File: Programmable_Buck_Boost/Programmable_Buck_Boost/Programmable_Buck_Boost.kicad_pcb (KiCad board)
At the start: 2 copper layers, 29 parts, among them J2 DC INPUT, Q5 IRF3205, Q6 IRF3205, Q7 2N7002, U4 TL494, U6 IR2101

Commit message: Finalize Schematic
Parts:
- added C1: C0603/1nF, Capacitor_SMD:C_0603_1608Metric, F.Cu at (160.4, 80.4)
- added C10: C0805/22uF, Capacitor_SMD:C_0603_1608Metric, F.Cu at (191.1, 112.2)
- added C11: C0603/0.1uF, Capacitor_SMD:C_0603_1608Metric, F.Cu at (191.1, 114.7)
- added C13: C0805/22uF, Capacitor_SMD:C_0603_1608Metric, F.Cu at (191.1, 117.2)
- added C14: C0805/22uF, Capacitor_SMD:C_0603_1608Metric, F.Cu at (191.1, 119.7)
- added C15: C0603/10uF, Capacitor_SMD:C_0603_1608Metric, F.Cu at (160.4, 93.0)
- added C16: C0603/470nF, Capacitor_SMD:C_0603_1608Metric, F.Cu at (164.4, 80.4)
- added C17: C0603/100nF, Capacitor_SMD:C_0603_1608Metric, F.Cu at (164.4, 82.9)
- added C18: C0603/68pF, Capacitor_SMD:C_0603_1608Metric, F.Cu at (164.4, 85.4)
- added C19: C0603/1uF, Capacitor_SMD:C_0603_1608Metric, F.Cu at (164.4, 87.9)
- added C2: C0603/100nF, Capacitor_SMD:C_0603_1608Metric, F.Cu at (144.6, 127.5)
- added C2: C0603/10uF, Capacitor_SMD:C_0603_1608Metric, F.Cu at (160.4, 82.9)
- added C21: C0603/100nF, Capacitor_SMD:C_0603_1608Metric, F.Cu at (164.4, 90.5)
- added C22: C0603/1uF, Capacitor_SMD:C_0603_1608Metric, F.Cu at (191.1, 122.2)
- added C3: C0603/1uF, Capacitor_SMD:C_0603_1608Metric, F.Cu at (160.4, 85.4)
- added C4: C0603/0.1uF, Capacitor_SMD:C_0603_1608Metric, F.Cu at (160.4, 87.9)
- added C5: C0603/0.1uF, Capacitor_SMD:C_0603_1608Metric, F.Cu at (160.4, 90.5)
- added C5: C0603/100nF, Capacitor_SMD:C_0603_1608Metric, F.Cu at (144.6, 130.1)
- added C6: C0603/10uF, Capacitor_SMD:C_0603_1608Metric, F.Cu at (144.6, 132.6)
- added C7: C0603/1uF, Capacitor_SMD:C_0603_1608Metric, F.Cu at (144.6, 135.1)
- added C8: C0603/10uF, Capacitor_SMD:C_0603_1608Metric, F.Cu at (144.6, 137.6)
- added C9: C0805/22uF, Capacitor_SMD:C_0603_1608Metric, F.Cu at (191.1, 109.7)
- added D2: SS34, Diode_SMD:D_SMA, F.Cu at (174.6, 126.0)
- added R1: R0603/4.7K, Resistor_SMD:R_0603_1608Metric, F.Cu at (144.6, 140.1)
- added R10: R0603/100K, Resistor_SMD:R_0603_1608Metric, F.Cu at (195.1, 117.2)
- added R11: R0603/100K, Resistor_SMD:R_0603_1608Metric, F.Cu at (195.1, 119.7)
- added R2: R0603/100K, Resistor_SMD:R_0603_1608Metric, F.Cu at (148.6, 127.5)
- added R3: R0603/51K, Resistor_SMD:R_0603_1608Metric, F.Cu at (148.6, 130.1)
- added R4: R0603/100K, Resistor_SMD:R_0603_1608Metric, F.Cu at (148.6, 132.6)
- added R5: R0603/56k, Resistor_SMD:R_0603_1608Metric, F.Cu at (148.6, 135.1)
- added R6: R0603/4.7K, Resistor_SMD:R_0603_1608Metric, F.Cu at (148.6, 137.6)
- added R7: R0603/100K, Resistor_SMD:R_0603_1608Metric, F.Cu at (195.1, 109.7)
- added R8: R0603/100K, Resistor_SMD:R_0603_1608Metric, F.Cu at (195.1, 112.2)
- added R9: R0603/0.82, Resistor_SMD:R_0603_1608Metric, F.Cu at (195.1, 114.7)
- added SW1: RotaryEncoder_Switch, Rotary_Encoder:RotaryEncoder_Alps_EC11E-Switch_Vertical_H20mm, F.Cu at (119.8, 136.8)
- added U1: MP1470, Package_TO_SOT_SMD:TSOT-23-6, F.Cu at (153.2, 128.7)
- added U2: MSPS003F4SPW20R, Package_SO:TSSOP-20_4.4x6.5mm_P0.65mm, F.Cu at (169.0, 98.5)
- added U3: MCP601-xOT, Package_TO_SOT_SMD:SOT-23-5, F.Cu at (153.2, 133.3)
- added U5: EG1198, Package_SO:HSOP-8-1EP_3.9x4.9mm_P1.27mm_EP2.3x2.3mm, F.Cu at (163.1, 127.6)
- R36, R39, R40: value R0603/10k -> R0603/100k
- R37: value R0603/220R -> R0603/2.2K
- R53: value RS/0.5R -> RS/0.1R
- R55: value R0603/56k -> R0603/150K
- U4: footprint Package_DIP:CERDIP-16_W7.62mm_SideBrazed_LongPads -> Package_SO:SOIC-16_3.9x9.9mm_P1.27mm
- moved R36 48.7 mm to (140.5, 81.7)
- moved R37 48.7 mm to (140.5, 84.2)
- moved R38 48.7 mm to (140.5, 86.7)
- moved R39 48.7 mm to (140.5, 89.2)
- moved R40 48.7 mm to (140.5, 91.8)
- moved R41 48.7 mm to (144.5, 81.7)
- moved R42 48.7 mm to (144.5, 84.2)
- moved R43 48.7 mm to (144.5, 86.7)
- moved R44 48.7 mm to (144.5, 89.2)
- moved R45 48.7 mm to (144.5, 91.8)
- moved R51 48.7 mm to (152.5, 81.7)
- moved R52 48.7 mm to (152.5, 84.2)
- moved R53 48.7 mm to (152.5, 86.7)
- moved R54 48.7 mm to (152.5, 89.2)
- moved R55 48.7 mm to (152.5, 91.8)
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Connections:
- R36 pad 1: Net-(C17-Pad2) -> /I_SET
- R37 pad 2: Net-(C17-Pad2) -> /I_SET
- R39 pad 1: Net-(U4-1IN-) -> /V_SET
- R40 pad 2: Net-(U4-1IN-) -> /V_SET
- R52 pad 1: V_set -> /V_FB
- R53 pad 2: I_set -> Net-(C20-Pad2)
- R55 pad 1: V_set -> /V_FB
- U4 pad 1: V_fb -> /V_FB
- U4 pad 15: Net-(U4-1IN-) -> /I_SET
- U4 pad 16: I_set -> /I_FB
- U4 pad 2: Net-(U4-1IN-) -> /V_SET

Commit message: Change design
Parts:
- added C11: Cp/470uF/63V, Capacitor_THT:CP_Radial_D12.5mm_P5.00mm, F.Cu at (205.0, 119.6)
- added C12: Cp/47uF/63V, Capacitor_THT:CP_Radial_D8.0mm_P3.50mm, F.Cu at (234.7, 147.2)
- added C2: C0603/33nF, Capacitor_SMD:C_0603_1608Metric, F.Cu at (216.5, 113.8)
- added C20: 220uF/65V, Connector_JST:JST_XH_B5B-XH-AM_1x05_P2.50mm_Vertical, F.Cu at (218.0, 133.5)
- added C22: Cp/470uF/63V, Capacitor_THT:CP_Radial_D12.5mm_P5.00mm, F.Cu at (205.0, 133.7)
- added C23: Cp/470uF/63V, Capacitor_THT:CP_Radial_D12.5mm_P5.00mm, F.Cu at (205.0, 147.7)
- added C24: C0603/1nF, Capacitor_SMD:C_0603_1608Metric, F.Cu at (216.5, 116.3)
- added C25: C0603/100nF, Capacitor_SMD:C_0603_1608Metric, F.Cu at (216.5, 118.8)
- added C26: C0603/100nF, Capacitor_SMD:C_0603_1608Metric, F.Cu at (216.5, 121.4)
- added C27: C0603/100nF, Capacitor_SMD:C_0603_1608Metric, F.Cu at (216.5, 123.9)
- added C28: C0603/100nF, Capacitor_SMD:C_0603_1608Metric, F.Cu at (216.5, 126.4)
- added C29: C0603/100nF, Capacitor_SMD:C_0603_1608Metric, F.Cu at (216.5, 128.9)
- added C30: C0603/100nF, Capacitor_SMD:C_0603_1608Metric, F.Cu at (220.5, 113.8)
- added C31: C0603/100nF, Capacitor_SMD:C_0603_1608Metric, F.Cu at (220.5, 116.3)
- added D3: SS34, Diode_SMD:D_SMA, F.Cu at (227.0, 148.0)
- added J1: Conn_01x05_Pin, Connector_JST:JST_XH_B5B-XH-AM_1x05_P2.50mm_Vertical, F.Cu at (218.0, 141.3)
- added J4: Conn_01x04_Pin, Connector_PinSocket_2.54mm:PinSocket_1x04_P2.54mm_Vertical, F.Cu at (233.8, 132.5)
- added L1: L/47uH /620mA, Inductor_SMD:L_Abracon_ASPI-0425, F.Cu at (229.6, 126.7)
- added R12: R0603/150K, Resistor_SMD:R_0603_1608Metric, F.Cu at (220.5, 121.4)
- added R13: R0603/150K, Resistor_SMD:R_0603_1608Metric, F.Cu at (220.5, 123.9)
- added R14: R0603/150K, Resistor_SMD:R_0603_1608Metric, F.Cu at (220.5, 126.4)
- added R15: R0603/150K, Resistor_SMD:R_0603_1608Metric, F.Cu at (220.5, 128.9)
- added R16: R0603/10K, Resistor_SMD:R_0603_1608Metric, F.Cu at (224.5, 113.8)
- added R17: R0603/10K, Resistor_SMD:R_0603_1608Metric, F.Cu at (224.5, 116.3)
- added R18: R0603/100K, Resistor_SMD:R_0603_1608Metric, F.Cu at (224.5, 118.8)
- added R19: R0603/100K, Resistor_SMD:R_0603_1608Metric, F.Cu at (224.5, 121.4)
- added R9: R0603/100K, Resistor_SMD:R_0603_1608Metric, F.Cu at (220.5, 118.8)
- added REF**: Untitled, Untitled, F.Cu at (125.8, 93.0)
- added U2: XL7005A, Package_SO:SOIC-8-1EP_3.9x4.9mm_P1.27mm_EP2.29x3mm, F.Cu at (218.7, 149.1)
- added U5: STM32F103C8Tx, Package_QFP:LQFP-48_7x7mm_P0.5mm, F.Cu at (232.2, 118.2)
- added U7: MCP601-xOT, Package_TO_SOT_SMD:SOT-23-5, F.Cu at (235.2, 126.3)
- C9: value C0805/22uF -> C0603/10uF
- D2: value SS34 -> SS24
- Q5, Q6: value IRF3205 -> IRFB4110PbF
- R10: value R0603/100K -> R0603/30K
- R11: value R0603/100K -> R0603/3.3K
- R37: value R0603/2.2K -> R0603/100K
- R53: value RS/0.1R -> RS/0.002R
- R7: value R0603/100K -> R0603/75K
- R8: value R0603/100K -> R0603/24K
- moved U6 66.1 mm to (179.7, 85.4), turned to 90 degrees
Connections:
- C10 pad 1: Net-(U1-IN) -> +12V
- C13 pad 1: Net-(C13-Pad1) -> +12V
- C14 pad 1: Net-(C13-Pad1) -> +12V
- C9 pad 1: Net-(C9-Pad1) -> +3.3V
- R10 pad 1: /12VFB -> +12V
- R10 pad 2: Net-(C13-Pad1) -> /12VFB
- R2 pad 2: Net-(U1-IN) -> +12V
- R44 pad 2: +5V -> +12V
- R6 pad 1: /VSETPOINT -> /V_PWM
- R7 pad 1: /3V3FB -> +3.3V
- R7 pad 2: Net-(C9-Pad1) -> /3V3FB
- SW1 pad A: Net-(U2-PA25/A2) -> /ENC_A
- SW1 pad B: Net-(U2-PA24/A3) -> /ENC_B
- U1 pad 3: Net-(U1-IN) -> +12V
- U4 pad 10: Net-(U4-E1) -> Net-(Q7-G)
- U4 pad 9: Net-(U4-E1) -> Net-(Q7-G)

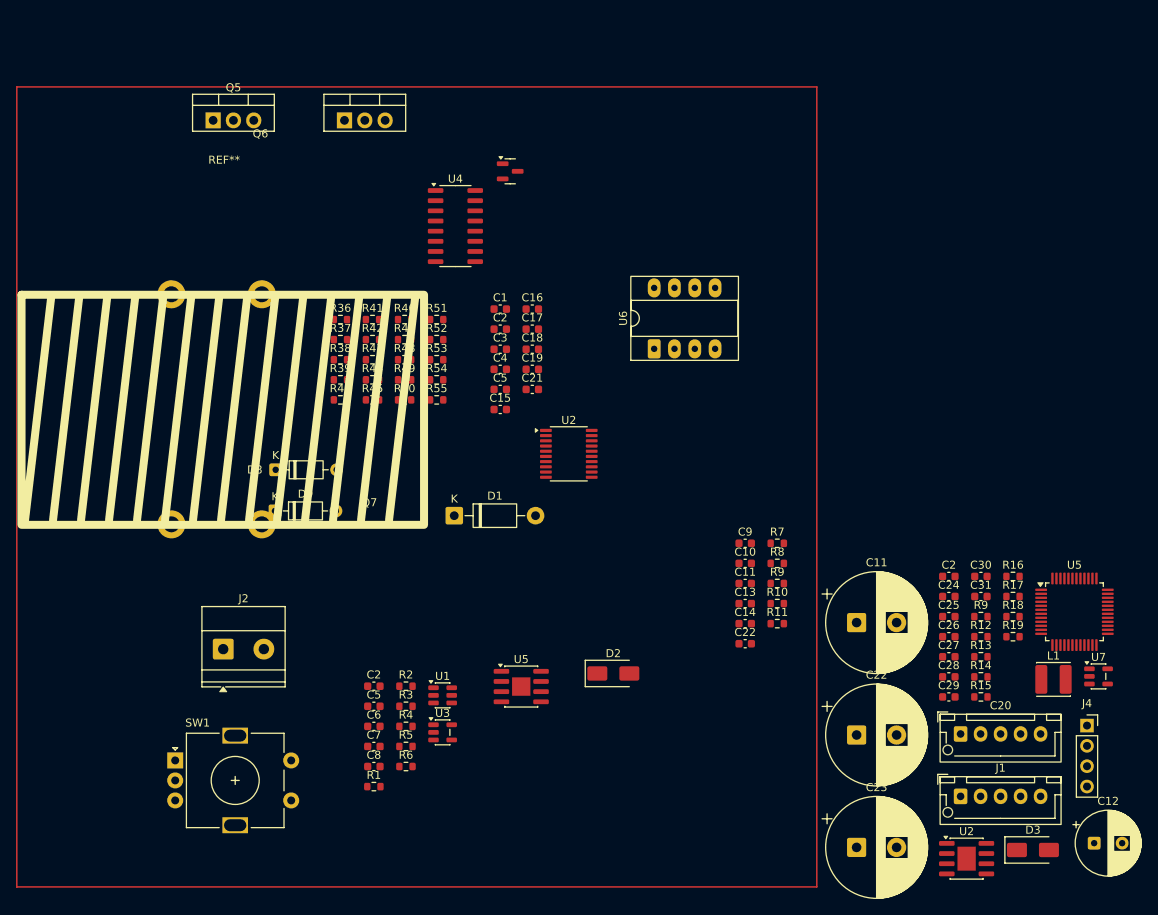
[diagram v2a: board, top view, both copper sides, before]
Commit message: Place component on board
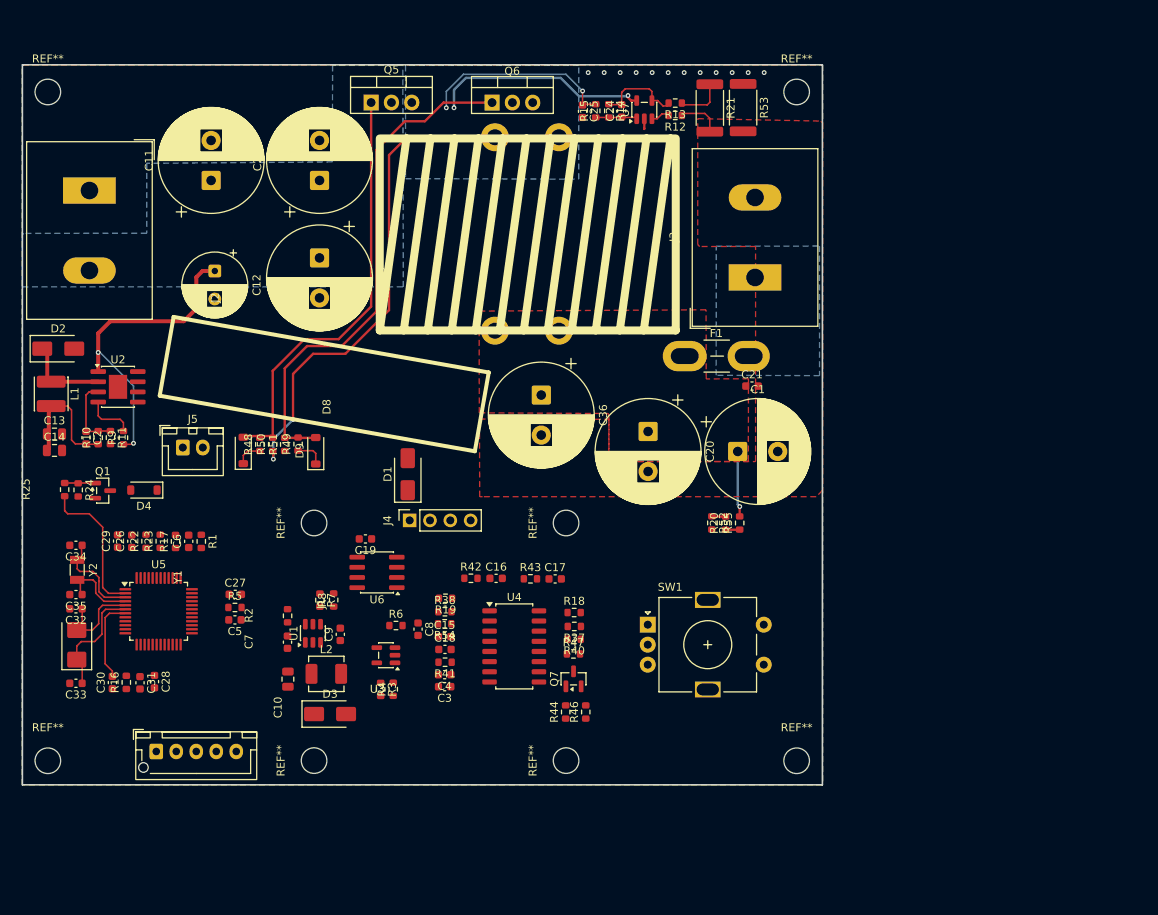
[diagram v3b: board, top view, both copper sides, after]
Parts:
- removed the C11 at (191.1, 114.7)
- removed the C2 at (144.6, 127.5)
- removed the C2 at (216.5, 113.8)
- removed the C2 at (160.4, 82.9)
- removed the C22 at (191.1, 122.2)
- removed the C5 at (160.4, 90.5)
- removed the C5 at (144.6, 130.1)
- removed R36, R39: R0603/100k, Resistor_SMD:R_0603_1608Metric
- removed R45: R0603/4.7k, Resistor_SMD:R_0603_1608Metric
- removed the R9 at (195.1, 114.7)
- removed the R9 at (220.5, 118.8)
- removed the REF** at (125.8, 93.0)
- removed the U2 at (218.7, 149.1)
- removed the U2 at (169.0, 98.5)
- removed the U5 at (232.2, 118.2)
- removed the U5 at (163.1, 127.6)
- added C2: C0603/33nF, Capacitor_SMD:C_0603_1608Metric, F.Cu at (108.7, 96.5)
- added C32: C0603/20pF, Capacitor_SMD:C_0603_1608Metric, F.Cu at (107.4, 117.9)
- added C33: C0603/20pF, Capacitor_SMD:C_0603_1608Metric, F.Cu at (107.4, 127.2)
- added C34: C0603/20pF, Capacitor_SMD:C_0603_1608Metric, F.Cu at (107.4, 109.9)
- added C35: C0603/20pF, Capacitor_SMD:C_0603_1608Metric, F.Cu at (107.4, 116.1)
- added C36: Cp/680uF/63V, Capacitor_THT:CP_Radial_D13.0mm_P5.00mm, F.Cu at (165.6, 91.2)
- added C5: C0603/100nF, Capacitor_SMD:C_0603_1608Metric, F.Cu at (127.3, 119.3)
- added D4: 1N4148W, Diode_SMD:D_SOD-123, F.Cu at (115.9, 103.0)
- added F1: Fuse, Fuse:Fuse_Blade_Mini_directSolder, F.Cu at (183.5, 86.3)
- added J3: DC OUTPUT, TerminalBlock_Dinkle:TerminalBlock_Dinkle_DT-55-B01X-02_P10.00mm, F.Cu at (192.3, 76.5)
- added J5: FAN, Connector_JST:JST_XH_B2B-XH-A_1x02_P2.50mm_Vertical, F.Cu at (120.8, 97.7)
- added L2: 4.7uH, Inductor_SMD:L_APV_APH0412, F.Cu at (138.7, 126.0)
- added L3: 68uF/25A, Programmable_Buck:Inductor_36x23x15MM, F.Cu at (163.9, 71.1)
- added Q1: 2N7002, Package_TO_SOT_SMD:SOT-23, F.Cu at (110.7, 103.1)
- added R20: R0603/10k, Resistor_SMD:R_0603_1608Metric, F.Cu at (188.6, 107.2)
- added R21: R2512/0.002R/3W, Resistor_SMD:R_2512_6332Metric, F.Cu at (186.6, 55.3)
- added R22: R0603/10K, Resistor_SMD:R_0603_1608Metric, F.Cu at (116.2, 109.4)
- added R23: R0603/10K, Resistor_SMD:R_0603_1608Metric, F.Cu at (117.9, 109.4)
- added R24: R0603/10K, Resistor_SMD:R_0603_1608Metric, F.Cu at (107.7, 103.0)
- added R25: R0603/10K, Resistor_SMD:R_0603_1608Metric, F.Cu at (106.0, 103.0)
- added R9: R0603/100K, Resistor_SMD:R_0603_1608Metric, F.Cu at (113.3, 96.5)
- added REF**: MountingHole_3.2mm_M3, MountingHole:MountingHole_3.2mm_M3, F.Cu at (197.5, 136.9)
- added REF**: MountingHole_3.2mm_M3, MountingHole:MountingHole_3.2mm_M3, F.Cu at (103.9, 136.9)
- added REF**: MountingHole_3.2mm_M3, MountingHole:MountingHole_3.2mm_M3, F.Cu at (197.5, 53.3)
- added REF**: MountingHole_3.2mm_M3, MountingHole:MountingHole_3.2mm_M3, F.Cu at (137.2, 136.8)
- added REF**: MountingHole_3.2mm_M3, MountingHole:MountingHole_3.2mm_M3, F.Cu at (168.7, 136.8)
- added REF**: MountingHole_3.2mm_M3, MountingHole:MountingHole_3.2mm_M3, F.Cu at (137.2, 107.2)
- added REF**: MountingHole_3.2mm_M3, MountingHole:MountingHole_3.2mm_M3, F.Cu at (168.7, 107.2)
- added REF**: MountingHole_3.2mm_M3, MountingHole:MountingHole_3.2mm_M3, F.Cu at (103.9, 53.3)
- added U2: XL7005A, Package_SO:SOIC-8-1EP_3.9x4.9mm_P1.27mm_EP2.29x3mm, F.Cu at (112.7, 90.1)
- added U5: STM32F103C8Tx, Package_QFP:LQFP-48_7x7mm_P0.5mm, F.Cu at (117.7, 118.2)
- added Y1: 8Mhz, Crystal:Crystal_SMD_5032-2Pin_5.0x3.2mm, F.Cu at (107.5, 122.4)
- added Y2: 32.768K, Crystal:Crystal_SMD_3215-2Pin_3.2x1.5mm, F.Cu at (107.5, 113.0)
- C1: value C0603/1nF -> Cp/680uF/63V; footprint Capacitor_SMD:C_0603_1608Metric -> Capacitor_THT:CP_Radial_D13.0mm_P5.00mm
- C10, C13, C14: footprint Capacitor_SMD:C_0603_1608Metric -> Capacitor_SMD:C_0805_2012Metric
- C11, C22, C23: value Cp/470uF/63V -> Cp/680uF/63V; footprint Capacitor_THT:CP_Radial_D12.5mm_P5.00mm -> Capacitor_THT:CP_Radial_D13.0mm_P5.00mm
- C18: value C0603/68pF -> C0603/150pF
- C20: value 220uF/65V -> Cp/680uF/63V; footprint Connector_JST:JST_XH_B5B-XH-AM_1x05_P2.50mm_Vertical -> Capacitor_THT:CP_Radial_D13.0mm_P5.00mm
- C21: value C0603/100nF -> C0603/100nF/50V
- D1: value 1N5819 -> SS24; footprint Diode_THT:D_DO-41_SOD81_P10.16mm_Horizontal -> Diode_SMD:D_SMA
- D3: value SS34 -> SS24
- D8: value 1N4148 -> 1N4148W; footprint Diode_THT:D_DO-35_SOD27_P7.62mm_Horizontal -> Diode_SMD:D_SOD-123
- D9: footprint Diode_THT:D_DO-35_SOD27_P7.62mm_Horizontal -> Diode_SMD:D_SOD-123
- J1: value Conn_01x05_Pin -> DEBUG
- J2: footprint TerminalBlock_Phoenix:TerminalBlock_Phoenix_MKDS-1,5-2-5.08_1x02_P5.08mm_Horizontal -> TerminalBlock_Dinkle:TerminalBlock_Dinkle_DT-55-B01X-02_P10.00mm
- J4: value Conn_01x04_Pin -> LCD
- L1: value L/47uH /620mA -> L/47uH/620mA
- R12, R13, R15: value R0603/150K -> R0603/1K
- R14: value R0603/150K -> R0603/75K
- R41: value R0603/150K -> R0603/100K
- R53: value RS/0.002R -> R2512/0.002R/3W; footprint Resistor_SMD:R_0603_1608Metric -> Resistor_SMD:R_2512_6332Metric
- U4: footprint Package_SO:SOIC-16_3.9x9.9mm_P1.27mm -> Package_SO:SOP-16_4.4x10.4mm_P1.27mm
- U6: footprint Package_DIP:CERDIP-8_W7.62mm_SideBrazed_LongPads_Socket -> Package_SO:SOIC-8_3.9x4.9mm_P1.27mm
- moved C12 131.1 mm to (124.8, 75.7), turned to -90 degrees
- moved L1 130.3 mm to (104.3, 91.0), turned to -90 degrees
- moved R16 111.6 mm to (113.7, 127.1), turned to 90 degrees
- moved C30 109.4 mm to (112.0, 127.1), turned to 90 degrees
- moved C29 105.7 mm to (112.6, 109.4), turned to 90 degrees
- moved C31 105.7 mm to (115.4, 127.1), turned to -90 degrees
- moved R17 104.9 mm to (119.8, 109.5), turned to 90 degrees
- moved C26 102.8 mm to (114.4, 109.4), turned to 90 degrees
- moved J1 100.7 mm to (117.4, 135.7)
- moved C23 99.7 mm to (137.8, 74.0), turned to -90 degrees
- moved C28 99.3 mm to (117.2, 127.0), turned to -90 degrees
- moved C11 97.8 mm to (124.3, 64.3), turned to 90 degrees
- moved C22 96.5 mm to (137.8, 64.3), turned to 90 degrees
- moved U7 90.8 mm to (178.4, 55.5), turned to 90 degrees
- moved C27 89.5 mm to (127.3, 116.1)
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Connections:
- C1 pad 1: /V_FB -> Net-(C1-Pad1)
- C1 pad 2: GND -> Net-(J3-Pin_2)
- C20 pad 1: Net-(C20-Pad1) -> Net-(C1-Pad1)
- C20 pad 2: Net-(C20-Pad2) -> Net-(J3-Pin_2)
- C21 pad 1: Net-(C20-Pad1) -> Net-(C1-Pad1)
- C21 pad 2: Net-(C20-Pad2) -> Net-(J3-Pin_2)
- J4 pad 3: /I2C0_SCL -> /SCL
- J4 pad 4: /I2C0_SDA -> /SDA
- R12 pad 1: Net-(C20-Pad2) -> Net-(J3-Pin_2)
- R52 pad 1: /V_FB -> /V_fb
- R53 pad 2: Net-(C20-Pad2) -> Net-(J3-Pin_2)
- R55 pad 2: Net-(C20-Pad1) -> Net-(C1-Pad1)
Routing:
- net Net-(D9-A): track 0.00 -> 64.1 mm
- net Net-(Q5-S): track 0.00 -> 61.6 mm, vias 0 -> 2
- net Net-(D8-A): track 0.00 -> 53.3 mm
- net VCC: track 0.00 -> 39.5 mm, vias 0 -> 2
- net +3.3V: track 0.00 -> 27.2 mm, vias 0 -> 2
- net /I_FB: track 0.00 -> 24.3 mm, vias 0 -> 2
- net /FAN_ON: track 0.00 -> 18.1 mm
- net +12V: track 0.00 -> 15.7 mm
- net Net-(U5-PD1): track 0.00 -> 14.5 mm
- net Net-(U5-PC14): track 0.00 -> 11.9 mm
- net Net-(U5-PD0): track 0.00 -> 11.3 mm
- net Net-(U7--): track 0.00 -> 11.0 mm
- net Net-(D2-K): track 0.00 -> 10.5 mm
- net /NRST: track 0.00 -> 10.5 mm
- net Net-(U5-PC15): track 0.00 -> 9.99 mm
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- added copper zone on B.Cu, net GND
- added copper zone on F.Cu, net GND
- added copper zone on F.Cu, net Net-(C1-Pad1)
- added copper zone on B.Cu, net Net-(J3-Pin_1)
- added copper zone on F.Cu, net Net-(J3-Pin_2)
- added copper zone on B.Cu, net Net-(Q5-S)
- added copper zone on B.Cu, net VCC
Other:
- board outline added: 100 x 90 mm

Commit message: Finalize PCb
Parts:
- added REF**: Screw_Generic_2.0x3.0mm_SilkScreen, Symbol:Screw_Generic_2.0x3.0mm_SilkScreen, F.Cu at (137.5, 89.7)
- moved C33 52.8 mm to (159.8, 133.0), turned to -90 degrees
- moved R46 49.0 mm to (122.1, 130.7), turned to 180 degrees
- moved Y1 48.7 mm to (155.0, 132.9), turned to 180 degrees
- moved C30 47.8 mm to (159.7, 129.7), turned to 180 degrees
- moved R37 47.5 mm to (122.2, 121.0)
- moved C18 47.5 mm to (106.0, 124.0)
- moved R43 47.5 mm to (116.7, 115.2)
- moved R54 47.5 mm to (106.0, 120.8)
- moved U4 47.5 mm to (114.7, 123.6)
- moved C15 47.5 mm to (106.0, 122.4)
- moved C16 47.5 mm to (112.4, 115.1)
- moved C3 47.5 mm to (106.0, 128.7)
- moved C4 47.5 mm to (106.0, 127.2)
- moved Q7 47.5 mm to (122.1, 127.7)
- moved R19 47.5 mm to (106.1, 117.6)
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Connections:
- U5 pad 2: /FAN_ON -> unconnected-(U5-PC13-Pad2)
- U5 pad 38: unconnected-(U5-PA15-Pad38) -> /FAN_ON
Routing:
- net +3.3V: track 27.2 -> 288.4 mm, vias 2 -> 8
- net +12V: track 15.7 -> 163.8 mm, vias 0 -> 6
- net /I_FB: track 24.3 -> 150.0 mm, vias 2 -> 3
- net /V_FB: track 1.77 -> 110.3 mm, vias 0 -> 2
- net /ENC_BUTTON: track 0.00 -> 64.1 mm, vias 0 -> 1
- net Net-(Q7-G): track 0.00 -> 63.2 mm, vias 0 -> 3
- net /V_fb: track 1.73 -> 52.4 mm, vias 0 -> 2
- net Net-(Q7-D): track 0.00 -> 50.6 mm, vias 0 -> 2
- net /SWDIO: track 0.00 -> 41.8 mm, vias 0 -> 2
- net /SCL: track 0.00 -> 40.9 mm, vias 0 -> 2
- net /SDA: track 0.00 -> 38.9 mm, vias 0 -> 2
- net /I_SET: track 0.00 -> 38.8 mm, vias 0 -> 2
- net /ENC_B: track 0.00 -> 37.3 mm, vias 0 -> 1
- net /ENC_A: track 0.00 -> 36.6 mm, vias 0 -> 1
- net /SWCLK: track 0.00 -> 36.5 mm, vias 0 -> 2
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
